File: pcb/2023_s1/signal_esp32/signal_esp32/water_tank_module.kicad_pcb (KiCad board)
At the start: 2 copper layers, 14 parts, among them J1 Conn_01x05_Male, J2 Conn_01x02_Male, U4 NRF24L01_Breakout

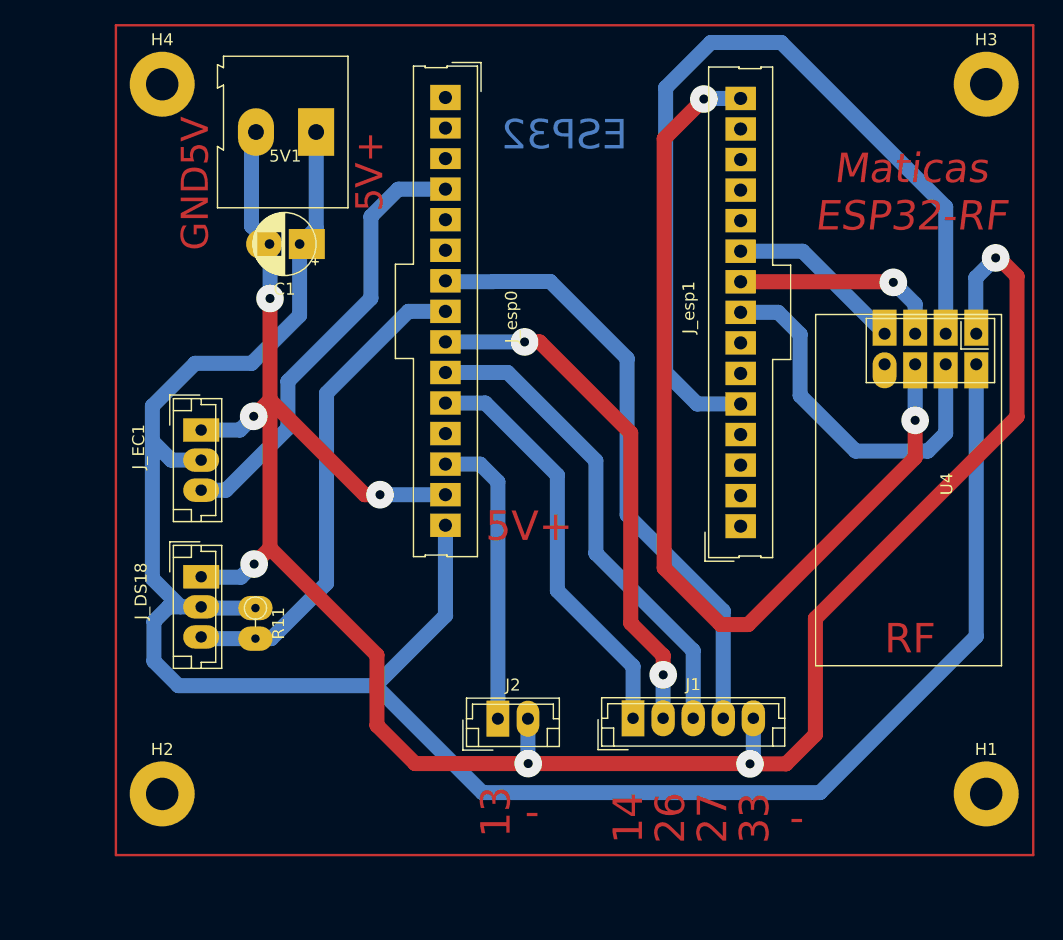
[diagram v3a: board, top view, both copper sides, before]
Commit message: update, changed some terminals to screw terminals for easyer connection
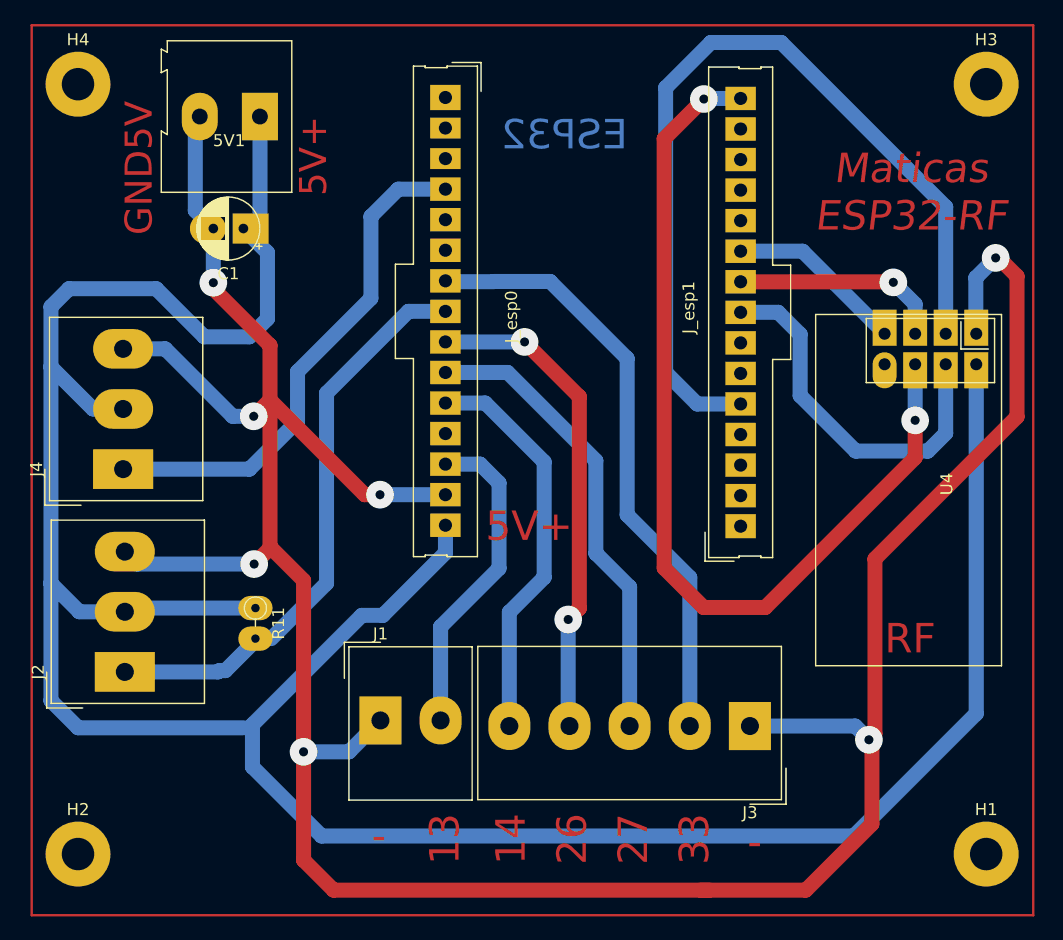
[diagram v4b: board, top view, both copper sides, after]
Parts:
- removed J_DS18, J_EC1: Conn_01x03_Male, Connector_JST:JST_EH_B3B-EH-A_1x03_P2.50mm_Vertical
- added J3: Screw_Terminal_01x05, TerminalBlock_Altech:Altech_AK300_1x05_P5.00mm_45-Degree, F.Cu at (175.6, 124.4)
- added J4: Screw_Terminal_01x03, TerminalBlock_Altech:Altech_AK300_1x03_P5.00mm_45-Degree, F.Cu at (123.5, 103.0)
- J1: value Conn_01x05_Male -> Screw_Terminal_01x02; footprint Connector_JST:JST_EH_B5B-EH-A_1x05_P2.50mm_Vertical -> TerminalBlock_Altech:Altech_AK300_1x02_P5.00mm_45-Degree
- J2: value Conn_01x02_Male -> Screw_Terminal_01x03; footprint Connector_JST:JST_EH_B2B-EH-A_1x02_P2.50mm_Vertical -> TerminalBlock_Altech:Altech_AK300_1x03_P5.00mm_45-Degree
- moved J2 31.3 mm to (123.6, 119.9), turned to 90 degrees
- moved J1 21.0 mm to (144.9, 123.9)
- moved H2 8.60 mm to (119.8, 135.0)
- moved H4 7.00 mm to (119.8, 71.0)
- moved H1 5.00 mm to (195.2, 135.0)
- moved 5V1 4.85 mm to (134.9, 73.7)
- moved C1 4.85 mm to (133.5, 83.0)
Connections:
- J1 pad 1: D14 -> GND5V
- J1 pad 2: D26 -> D13
- J2 pad 1: D13 -> D25
- J2 pad 2: GND5V -> 5v
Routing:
- net 5v: track 182.2 -> 236.3 mm
- net GND5V: track 186.7 -> 240.5 mm
- net D25: track 41.1 -> 47.1 mm
- net D34: track 36.9 -> 42.8 mm
- net D26: track 43.4 -> 41.1 mm
- net D13: track 25.1 -> 26.9 mm
- net D27: track 40.3 -> 38.8 mm
- net D14: track 34.6 -> 33.4 mm
- net D23: track 79.7 -> 78.6 mm
- net D33: track 51.0 -> 50.5 mm

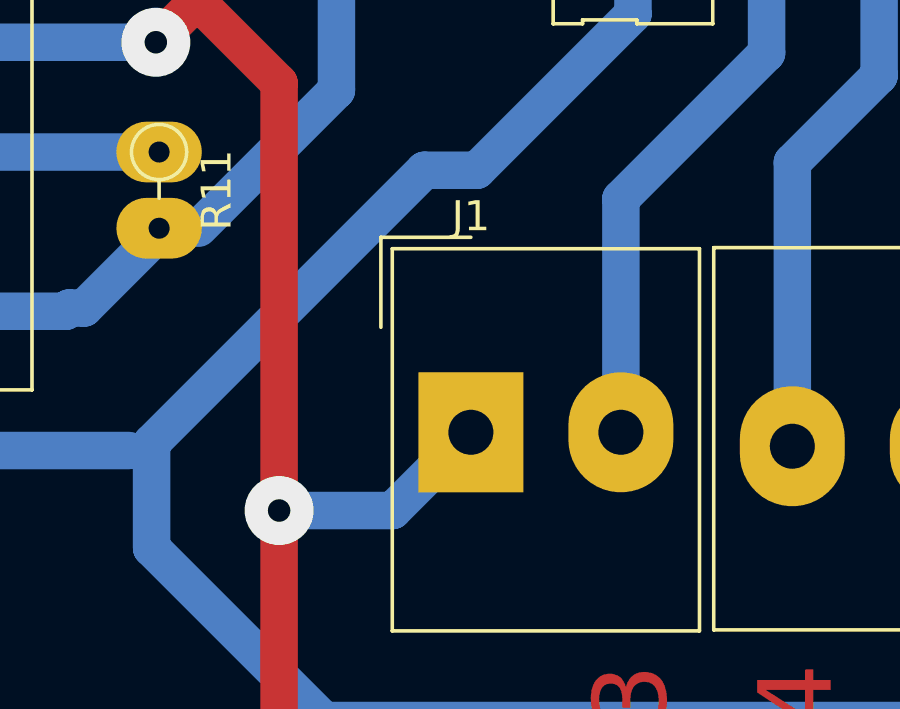
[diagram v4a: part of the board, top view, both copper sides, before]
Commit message: update, routed lights pcb
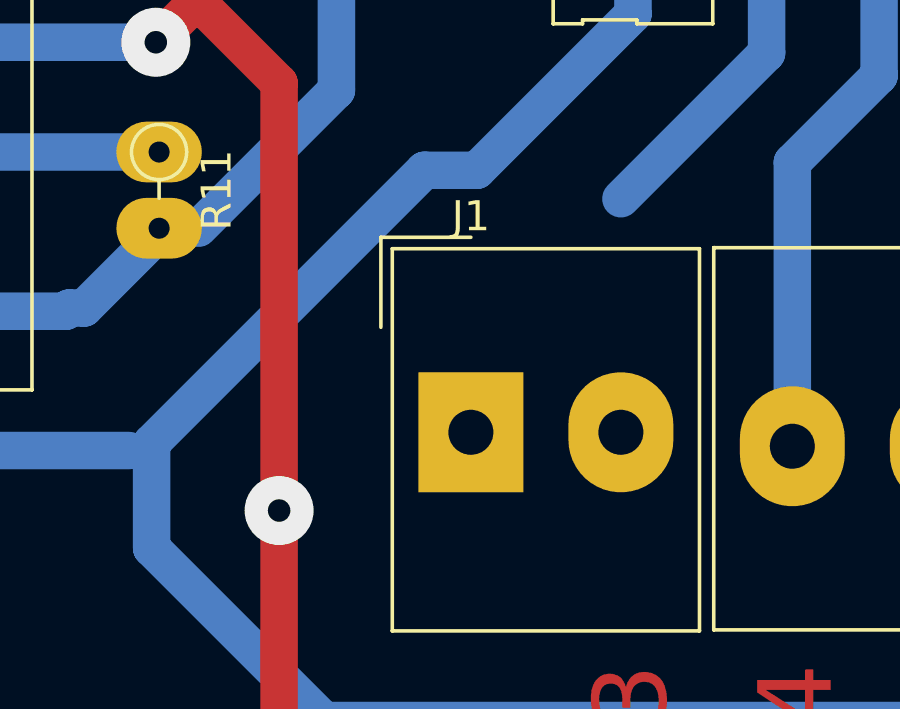
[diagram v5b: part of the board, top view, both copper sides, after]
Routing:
- net D13: track 26.9 -> 19.1 mm
- net GND5V: track 240.5 -> 233.0 mm
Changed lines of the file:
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@@
   (segment (start 154.75 104.15) (end 153.185 102.585) (width 1.25) (layer "B.Cu") (net 13))
   (segment (start 149.8925 116.1075) (end 154.75 111.25) (width 1.25) (layer "B.Cu") (net 13))
-  (segment (start 149.8925 123.8925) (end 149.8925 116.1075) (width 1.25) (layer "B.Cu") (net 13))
   (segment (start 153.185 102.585) (end 150.295 102.585) (width 1.25) (layer "B.Cu") (net 13))
   (segment (start 191.883 81.2098) (end 191.883 91.744) (width 1.25) (layer "B.Cu") (net 18))
@@
   (segment (start 129.5 81.5) (end 130.999113 82.999113) (width 1.25) (layer "B.Cu") (net 30))
   (segment (start 124.676 110.891) (end 123.6425 109.8575) (width 1.25) (layer "B.Cu") (net 30))
-  (segment (start 138.5 126.5) (end 142.285 126.5) (width 1.25) (layer "B.Cu") (net 30))
   (segment (start 184.3575 124.3575) (end 175.6075 124.3575) (width 1.25) (layer "B.Cu") (net 30))
   (segment (start 127 93) (end 123.5 93) (width 1.25) (layer "B.Cu") (net 30))
@@
   (segment (start 194.386 91.707) (end 194.423 91.744) (width 1.25) (layer "B.Cu") (net 30))
   (segment (start 132.6065 98.6065) (end 127 93) (width 1.25) (layer "B.Cu") (net 30))
-  (segment (start 142.285 126.5) (end 144.8925 123.8925) (width 1.25) (layer "B.Cu") (net 30))
   (segment (start 194.386 87.091) (end 194.386 91.707) (width 1.25) (layer "B.Cu") (net 30))
   (segment (start 130.999113 87.500887) (end 130.999113 82.999113) (width 1.25) (layer "B.Cu") (net 30))

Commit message: update, renamed folders, and built simple control routine
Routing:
- net GND5V: track 233.0 -> 242.1 mm
- net D13: track 19.1 -> 26.9 mm
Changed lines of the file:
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@@
   (segment (start 154.75 111.25) (end 154.75 104.15) (width 1.25) (layer "B.Cu") (net 13))
   (segment (start 154.75 104.15) (end 153.185 102.585) (width 1.25) (layer "B.Cu") (net 13))
+  (segment (start 149.8925 116.1075) (end 149.8925 123.8925) (width 1.25) (layer "B.Cu") (net 13))
   (segment (start 149.8925 116.1075) (end 154.75 111.25) (width 1.25) (layer "B.Cu") (net 13))
   (segment (start 153.185 102.585) (end 150.295 102.585) (width 1.25) (layer "B.Cu") (net 13))
@@
   (segment (start 138.5 135.5) (end 138.5 112.25) (width 1.25) (layer "F.Cu") (net 30))
   (segment (start 180.2486 138) (end 185.75 132.4986) (width 1.25) (layer "F.Cu") (net 30))
+  (segment (start 145.8 124.8) (end 145.8 125.1) (width 1.25) (layer "F.Cu") (net 30))
   (segment (start 135.712 109.57) (end 135.712 97.251) (width 1.25) (layer "F.Cu") (net 30))
   (segment (start 197.815 86.964) (end 197.815 98.648) (width 1.25) (layer "F.Cu") (net 30))
@@
   (segment (start 143.586 105.125) (end 135.712 97.251) (width 1.25) (layer "F.Cu") (net 30))
   (segment (start 186 110.463) (end 186 125) (width 1.25) (layer "F.Cu") (net 30))
+  (segment (start 144.8925 123.8925) (end 145.8 124.8) (width 1.25) (layer "F.Cu") (net 30))
   (segment (start 141 138) (end 138.5 135.5) (width 1.25) (layer "F.Cu") (net 30))
   (segment (start 135.712 92.712) (end 135.712 97.251) (width 1.25) (layer "F.Cu") (net 30))
@@
   (segment (start 124.676 110.891) (end 123.6425 109.8575) (width 1.25) (layer "B.Cu") (net 30))
   (segment (start 184.3575 124.3575) (end 175.6075 124.3575) (width 1.25) (layer "B.Cu") (net 30))
+  (segment (start 141.1075 123.8925) (end 138.5 126.5) (width 1.25) (layer "B.Cu") (net 30))
   (segment (start 127 93) (end 123.5 93) (width 1.25) (layer "B.Cu") (net 30))
   (segment (start 129.5 81.5) (end 129.5 74.059863) (width 1.25) (layer "B.Cu") (net 30))
@@
   (segment (start 194.386 91.707) (end 194.423 91.744) (width 1.25) (layer "B.Cu") (net 30))
   (segment (start 132.6065 98.6065) (end 127 93) (width 1.25) (layer "B.Cu") (net 30))
+  (segment (start 144.8925 123.8925) (end 141.1075 123.8925) (width 1.25) (layer "B.Cu") (net 30))
   (segment (start 194.386 87.091) (end 194.386 91.707) (width 1.25) (layer "B.Cu") (net 30))
   (segment (start 130.999113 87.500887) (end 130.999113 82.999113) (width 1.25) (layer "B.Cu") (net 30))

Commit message: update
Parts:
- moved R11 0.80 mm to (135.3, 114.6)
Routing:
- net D5: track 31.2 -> 35.9 mm
- net D25: track 47.1 -> 50.4 mm
- net 5v: track 236.3 -> 237.5 mm
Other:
- board text added: "25"
- board text added: "34"
- board text added: "5V"
- board text added: "GND"
